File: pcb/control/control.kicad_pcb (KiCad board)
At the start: 2 copper layers, 70 x 76 mm, 79 parts, among them J1 Conn_01x06, J10 Conn_01x02, J2 Conn_01x05, J3 Conn_01x01, J4 USB_B_Micro, J5 Conn_01x04, J6 Conn_01x06, J7 Conn_01x02, J8 Conn_01x02, J9 Conn_01x01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

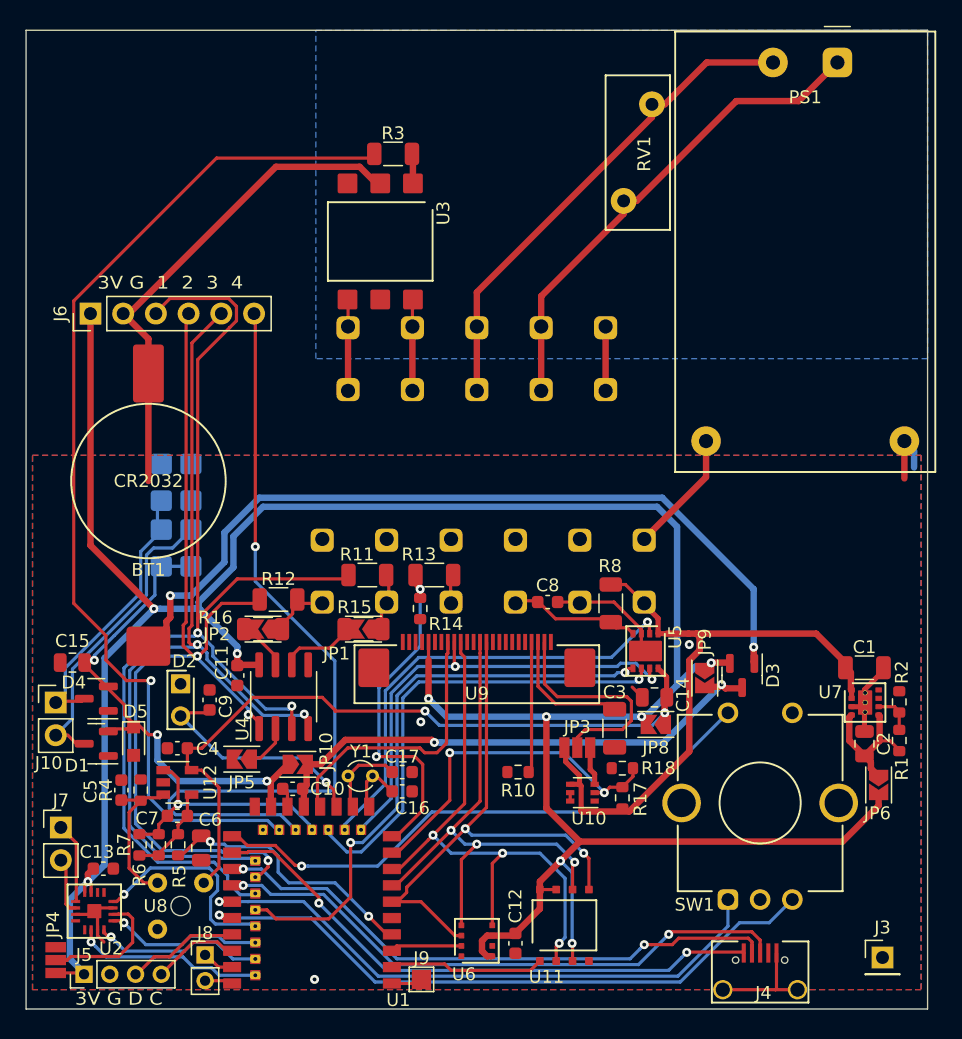
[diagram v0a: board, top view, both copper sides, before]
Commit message: Port symbol library to KiCad 6
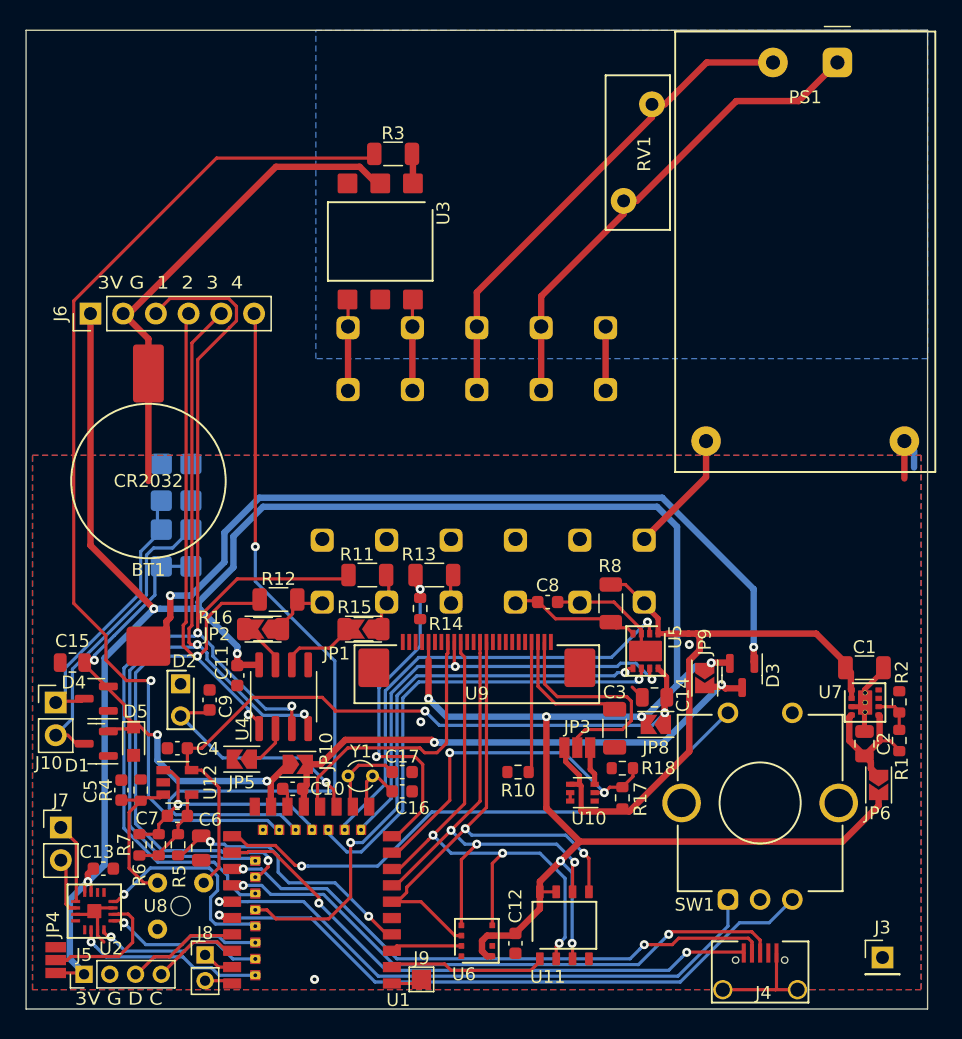
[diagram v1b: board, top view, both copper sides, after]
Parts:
- U11: footprint RoomControl:MR45V064B -> RoomControl:FM25CL64B
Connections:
- U9 pad 25: GND -> unconnected-(U9-Pad25)
- U9 pad 26: GND -> unconnected-(U9-Pad26)

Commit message: Minor fixes
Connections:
- U9 pad 25: unconnected-(U9-Pad25) -> GND
- U9 pad 26: unconnected-(U9-Pad26) -> GND
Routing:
- net GND: track 77.1 -> 83.5 mm
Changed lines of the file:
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@@
   (net 82 "unconnected-(U9-Pad15)")
   (net 83 "unconnected-(U9-Pad4)")
-  (net 84 "unconnected-(U9-Pad25)")
-  (net 85 "unconnected-(U9-Pad26)")
   (footprint "RoomControl:USB_Micro-B" (layer "F.Cu")
     (at 122 136.5)
@@
       (net 2 "GND") (pinfunction "GND") (pintype "power_in"))
     (pad "25" smd roundrect locked (at -8 -4.5 90) (size 3 2.4) (layers "F.Cu" "F.Paste" "F.Mask") (roundrect_rratio 0.1)
-      (net 84 "unconnected-(U9-Pad25)") (pinfunction "PAD") (pintype "no_connect") (solder_paste_margin -0.3))
+      (net 2 "GND") (pinfunction "PAD") (pintype "free") (solder_paste_margin -0.3))
     (pad "26" smd roundrect locked (at 8 -4.5 90) (size 3 2.4) (layers "F.Cu" "F.Paste" "F.Mask") (roundrect_rratio 0.1)
-      (net 85 "unconnected-(U9-Pad26)") (pinfunction "PAD") (pintype "no_connect") (solder_paste_margin -0.3))
+      (net 2 "GND") (pinfunction "PAD") (pintype "free") (solder_paste_margin -0.3))
   )
   (footprint "RoomControl:PEC12R" locked (layer "F.Cu")
@@
   (segment (start 70.55 130.15) (end 70.3 130.4) (width 0.25) (layer "F.Cu") (net 2))
   (segment (start 107.9 106.4) (end 108 106.5) (width 0.25) (layer "F.Cu") (net 2))
+  (segment (start 110.45 110.8) (end 110.45 112.35) (width 0.25) (layer "F.Cu") (net 2))
   (segment (start 112.775 108.85) (end 112.775 108.524002) (width 0.25) (layer "F.Cu") (net 2))
   (segment (start 84.925 120.9) (end 85.295 121.27) (width 0.25) (layer "F.Cu") (net 2))
   (segment (start 106.275 106.4) (end 107.9 106.4) (width 0.25) (layer "F.Cu") (net 2))
   (segment (start 72.54 84) (end 73 84) (width 0.5) (layer "F.Cu") (net 2))
+  (segment (start 111.05 110.2) (end 110.45 110.8) (width 0.25) (layer "F.Cu") (net 2))
   (segment (start 110.650998 106.4) (end 108.1 106.4) (width 0.25) (layer "F.Cu") (net 2))
   (segment (start 84.4 72.6) (end 90.9 72.6) (width 0.5) (layer "F.Cu") (net 2))
@@
   (segment (start 70.05 130.65) (end 70.3 130.4) (width 0.25) (layer "F.Cu") (net 2))
   (segment (start 74.5 88.65) (end 74.5 85.96) (width 0.5) (layer "F.Cu") (net 2))
+  (segment (start 111.1 113) (end 112.0625 113) (width 0.25) (layer "F.Cu") (net 2))
   (segment (start 70.55 130.65) (end 70.3 130.4) (width 0.25) (layer "F.Cu") (net 2))
   (segment (start 113.1 110.2) (end 112.775 109.875) (width 0.25) (layer "F.Cu") (net 2))
@@
   (segment (start 71.7375 130.15) (end 70.55 130.15) (width 0.25) (layer "F.Cu") (net 2))
   (segment (start 112.8625 113.8) (end 112.0625 113) (width 0.25) (layer "F.Cu") (net 2))
+  (segment (start 110.45 112.35) (end 111.1 113) (width 0.25) (layer "F.Cu") (net 2))
   (segment (start 74.5 85.96) (end 72.54 84) (width 0.5) (layer "F.Cu") (net 2))
   (segment (start 123.2 136.5) (end 119.1 136.5) (width 0.25) (layer "F.Cu") (net 2))
   (segment (start 108.1 106.4) (end 108 106.5) (width 0.25) (layer "F.Cu") (net 2))
+  (segment (start 113.1 110.2) (end 111.05 110.2) (width 0.25) (layer "F.Cu") (net 2))
   (segment (start 70.55 131.8375) (end 70.55 132.298022) (width 0.25) (layer "F.Cu") (net 2))
   (segment (start 73 84) (end 84.4 72.6) (width 0.5) (layer "F.Cu") (net 2))
